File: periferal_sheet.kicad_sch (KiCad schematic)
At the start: 0 parts

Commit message: Troquei o micro para STM32H523, adicionei o cristal HSE, circuito da fonte de 5V e 3v3, CAN, SD
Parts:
- added J3: Conn_02x02_Counter_Clockwise, symbol Connector_Generic:Conn_02x02_Counter_Clockwise
- added JP2: SolderJumper_2_Open, Jumper:SolderJumper-2_P1.3mm_Open_RoundedPad1.0x1.5mm, symbol Jumper:SolderJumper_2_Open
- added R24: 10K, Resistor_SMD:R_1206_3216Metric, symbol Device:R
- added R25: 120, Resistor_SMD:R_1206_3216Metric, symbol Device:R
- added U12: SN65HVD230, Package_SO:SOIC-8_3.9x4.9mm_P1.27mm, symbol Interface_CAN_LIN:SN65HVD230
- added U13: ~, Baja_Librarys:SD-CARD-GENERIC, symbol Baja_Librarys:SD-CARD-GENERIC
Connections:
- new net: R24.1, U12.8 (Rs)
- new net: JP2.2 (B), R25.2
- new net +12V: J3.1 (Pin_1)
- new net +3V3: U12.3 (VCC)
- new net 3V3: U13.4 (VCC)
- new net CAN +: J3.3 (Pin_3), R25.1, U12.7 (CANH)
- new net CAN -: J3.4 (Pin_4), JP2.1 (A), U12.6 (CANL)
- new net CRX: U12.4 (R)
- new net CS_SD: U13.2 (DAT3/CS)
- new net CTX: U12.1 (D)
- new net GND: J3.2 (Pin_2), R24.2, U12.2 (GND), U13.6 (GND)
- new net GNDD: U13.10 (SH_1), U13.11 (SH_2), U13.12 (SH_3), U13.13 (SH_4)
- new net MISO: U13.7 (DAT0/MISO)
- new net MOSI: U13.3 (CMD/MOSI)
- new net SCK: U13.5 (CLK)
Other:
- note added: "Conector Molex"
- note added: "Conector SD-Card"
- note added: "Nota: Par diferencial do CAN"
- note added: "Transceiver CAN"

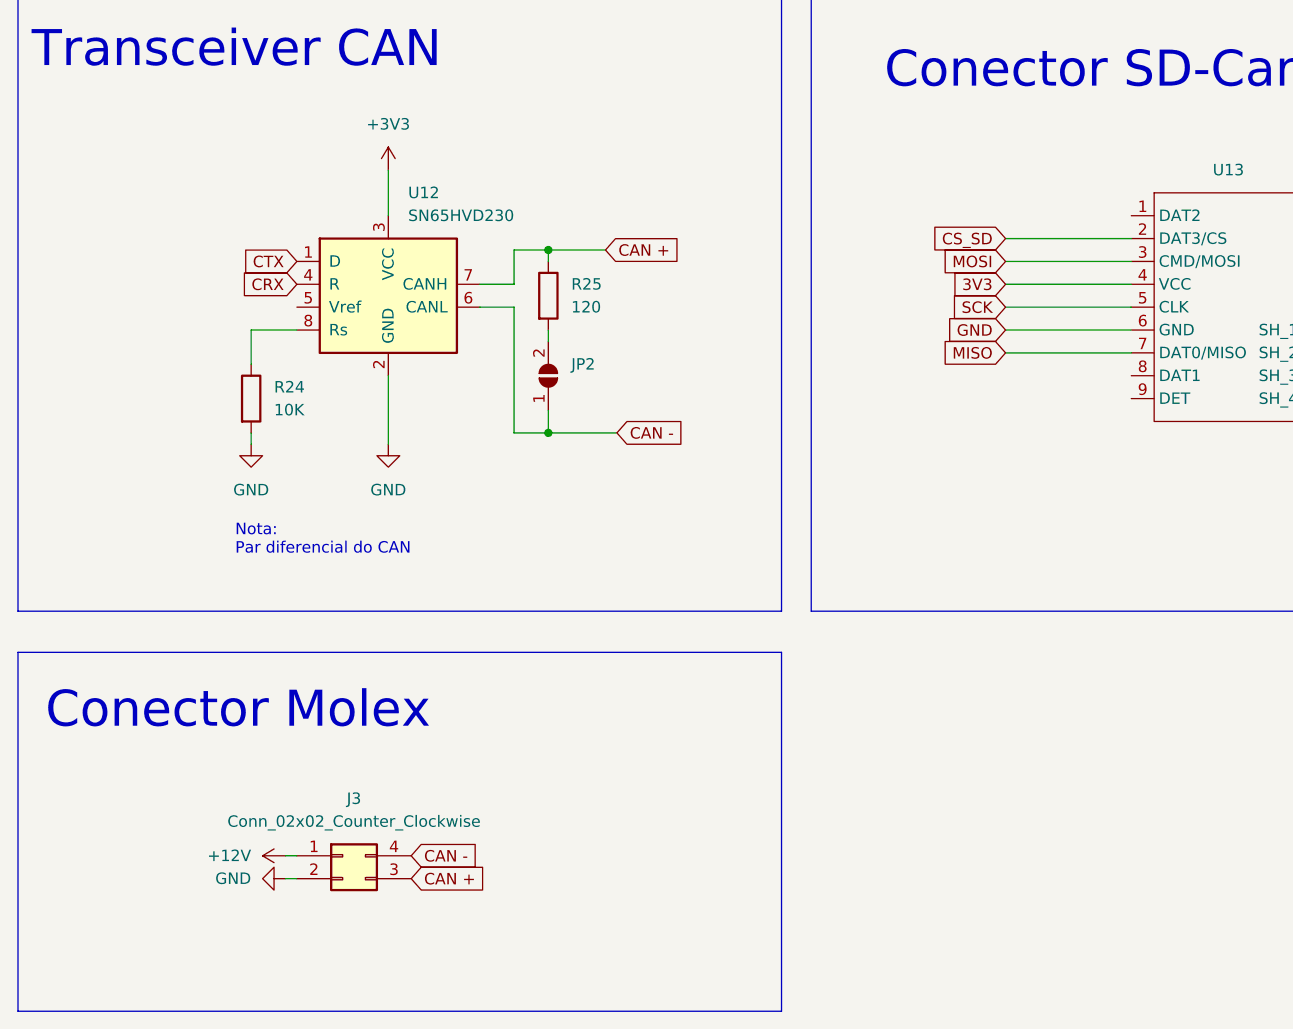
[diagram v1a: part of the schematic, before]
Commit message: Alterei o nome para o par diferencial do CAN, adicionei capacitores de desacoplamento para todas as alimentacoes
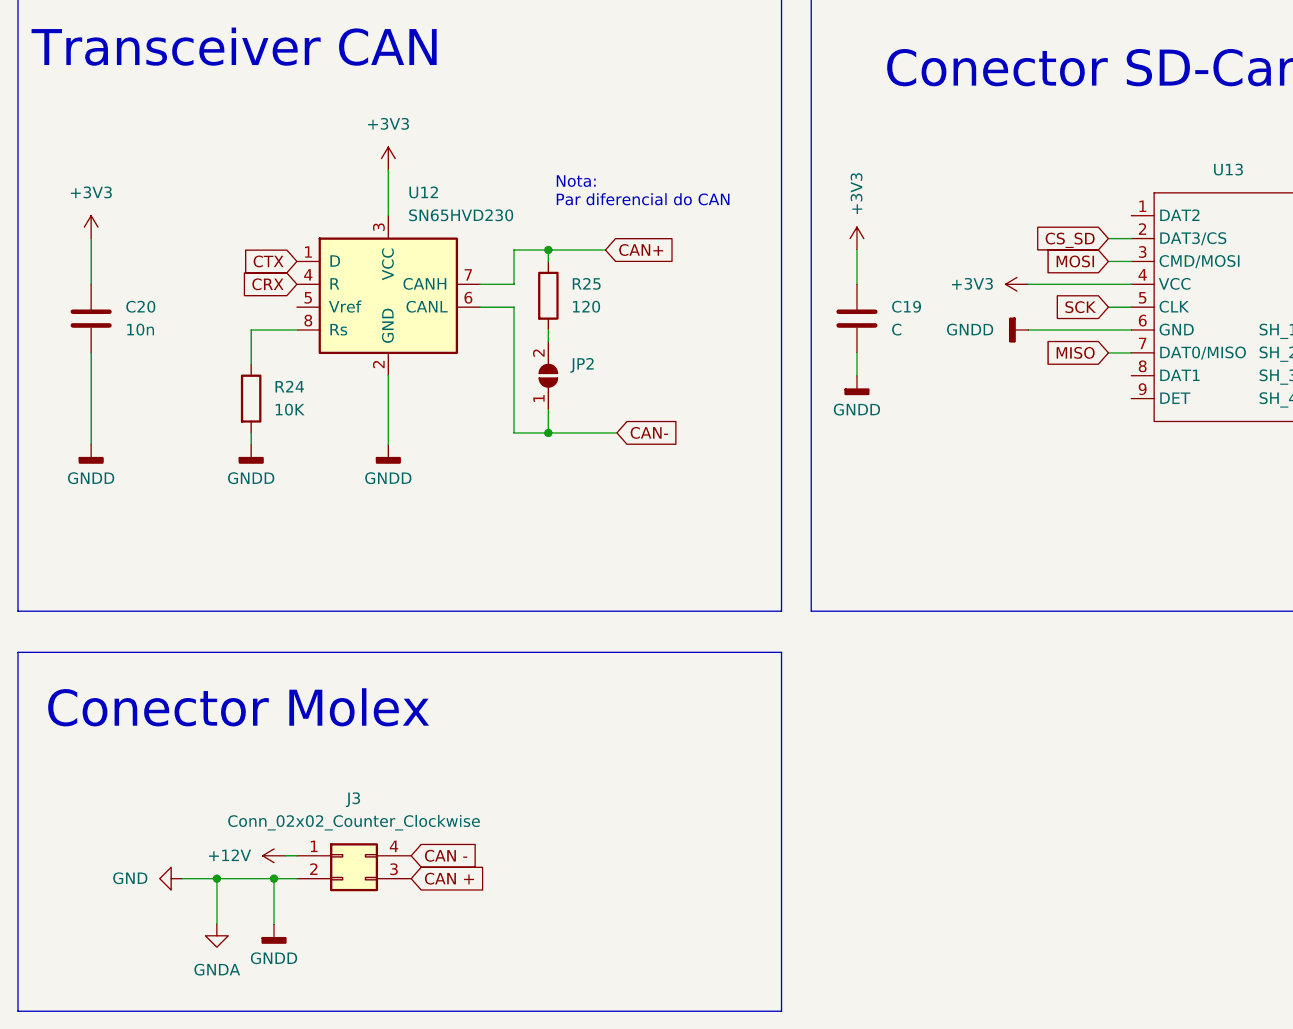
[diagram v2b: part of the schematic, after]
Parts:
- added C19: C, symbol Device:C
- added C20: 10n, symbol Device:C
- U13: footprint Baja_Librarys:SD-CARD-GENERIC -> BajaKICAD:SD-CARD-GENERIC
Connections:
- net 3V3 is gone; now on net +3V3: U13.4 (VCC)
- net GNDD is gone; now on net GND: U13.10 (SH_1), U13.11 (SH_2), U13.12 (SH_3), U13.13 (SH_4)
- net +3V3: now also C19.1, C20.1
- net CAN +: no longer R25.1, U12.7 (CANH)
- net CAN -: no longer JP2.1 (A), U12.6 (CANL)
- net GND: now also C19.2, C20.2
- new net CAN+: R25.1, U12.7 (CANH)
- new net CAN-: JP2.1 (A), U12.6 (CANL)

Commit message: Removi as entradas analógicas, projeto delas estava errado
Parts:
- removed J3: Conn_02x02_Counter_Clockwise, symbol Connector_Generic:Conn_02x02_Counter_Clockwise
- removed R25: 120, Resistor_SMD:R_1206_3216Metric, symbol Device:R
- added J3: Conn_02x02_Top_Bottom, Baja_Library:MX150L_4P, symbol Connector_Generic:Conn_02x02_Top_Bottom
- added R18: 120, Capacitor_SMD:C_0603_1608Metric_Pad1.08x0.95mm_HandSolder, symbol Device:R
- added R20: 10k, Resistor_SMD:R_1206_3216Metric_Pad1.30x1.75mm_HandSolder, symbol Device:R
- C19: renamed from C20; value 10n -> 1n; footprint (none) -> Capacitor_SMD:C_0603_1608Metric_Pad1.08x0.95mm_HandSolder
- C20: renamed from C19; value C -> 1n; footprint (none) -> Capacitor_SMD:C_0603_1608Metric_Pad1.08x0.95mm_HandSolder
- R19: renamed from R24; value 10K -> 10k; footprint Resistor_SMD:R_1206_3216Metric -> Resistor_SMD:R_1206_3216Metric_Pad1.30x1.75mm_HandSolder
- U13: footprint BajaKICAD:SD-CARD-GENERIC -> Baja_Library:SD-CARD-GENERIC
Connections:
- net +12V: now also J3.1 (Pin_1)
- net +3V3: now also R20.2
- net CAN+: now also J3.4 (Pin_4), R18.1
- net CAN-: now also J3.3 (Pin_3)
- net GND: now also J3.2 (Pin_2); no longer C19.2, C20.2, R19.2, U12.2 (GND), U13.10 (SH_1), U13.11 (SH_2), U13.12 (SH_3), U13.13 (SH_4), U13.6 (GND)
- net SD_ON: now reaches U13.9 (DET)
- net SD_ON: now also R20.1
- net at JP2.2 (B): now also R18.2
- new net GNDD: C19.2, C20.2, R19.2, U12.2 (GND), U13.10 (SH_1), U13.11 (SH_2), U13.12 (SH_3), U13.13 (SH_4), U13.6 (GND)
- no-connect marks 0 -> 2
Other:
- note added: "Nota: Permite diferentes tamanhos de resistor"
- note removed: "Nota: Par diferencial do CAN"
- moved on the sheet: JP2

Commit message: Alterei para ter 3 portas analogicas, adaptei o circuito do RPM para ter um jumper que permite usar como entrada digital
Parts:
- removed J3: Conn_02x02_Top_Bottom, Baja_Library:MX150L_4P, symbol Connector_Generic:Conn_02x02_Top_Bottom
- removed JP2: SolderJumper_2_Open, Jumper:SolderJumper-2_P1.3mm_Open_RoundedPad1.0x1.5mm, symbol Jumper:SolderJumper_2_Open
- removed R18: 120, Capacitor_SMD:C_0603_1608Metric_Pad1.08x0.95mm_HandSolder, symbol Device:R
- added C22, C24, C25: 22u, Capacitor_THT:CP_Radial_D6.3mm_P2.50mm, symbol Device:C
- added C23: 100n, Capacitor_SMD:C_0603_1608Metric_Pad1.08x0.95mm_HandSolder, symbol Device:C
- added D5: LED, Baja_Library:LED_1210_HandSoldering, symbol Device:LED
- added J2: Conn_02x06_Top_Bottom, Baja_Library:MX120G, symbol Connector_Generic:Conn_02x06_Top_Bottom
- added R15: 1k, Resistor_SMD:R_1206_3216Metric_Pad1.30x1.75mm_HandSolder, symbol Device:R
- added R16: 120, Capacitor_SMD:C_0603_1608Metric_Pad1.08x0.95mm_HandSolder, symbol Device:R
- added U10: AMS1117-3.3, Package_TO_SOT_SMD:SOT-223-3_TabPin2, symbol Regulator_Linear:AMS1117-3.3
- added U9: AMS1117-5.0, Package_TO_SOT_SMD:SOT-223-3_TabPin2, symbol Regulator_Linear:AMS1117-5.0
- renumbered C19 to C26, C20 to C27, R19 to R17, R20 to R18, U12 to U11, U13 to U12
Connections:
- net +12V: now also C22.1, J2.1 (Pin_1), U9.3 (VI)
- net +3V3: now also C25.1, R15.1, U10.2 (VO)
- net CAN+: now also J2.7 (Pin_7), R16.1
- net CAN-: now also J2.8 (Pin_8), R16.2
- net GND: now also C26.2, R17.2, U11.2 (GND), U12.10 (SH_1), U12.11 (SH_2), U12.12 (SH_3), U12.13 (SH_4), C22.2, C23.2, C24.2, C25.2, D5.1 (K), J2.2 (Pin_2), U10.1 (GND), U9.1 (GND)
- net GNDD: no longer C26.2, R17.2, U11.2 (GND), U12.10 (SH_1), U12.11 (SH_2), U12.12 (SH_3), U12.13 (SH_4)
- new net: D5.2 (A), R15.2
- new net +5V: C23.1, C24.1, U10.3 (VI), U9.2 (VO)
- new net CHASSI: J2.12 (Pin_12)
- new net MTMT: J2.6 (Pin_6)
- new net NTC_P1: J2.3 (Pin_3)
- new net NTC_P2: J2.4 (Pin_4)
- new net NTC_P3: J2.5 (Pin_5)
- new net OPTO_IN_0: J2.11 (Pin_11)
- new net OPTO_IN_1: J2.10 (Pin_10)
- new net OPTO_IN_2: J2.9 (Pin_9)
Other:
- note added: "Fonte 3V3 (LDO)"
- note added: "Fonte 5V (LDO)"
- note added: "LED da fonte"
- note added: "Nota: Capacitor "bulky" de desacoplamento é da entrada, o da saída já tem na fonte de 3v3"
- note added: "Nota: Capacitor 22uF recomendado pelo datasheet"
- note added: "Nota: Compatível com LDL1117 da ST"
- moved on the sheet: C26, C27, R17, R18, U11, U12

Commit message: Diminui o tamanho da placa
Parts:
- removed C27: 1n, Capacitor_SMD:C_0603_1608Metric_Pad1.08x0.95mm_HandSolder, symbol Device:C
- removed R18: 10k, Resistor_SMD:R_1206_3216Metric_Pad1.30x1.75mm_HandSolder, symbol Device:R
- removed U12: ~, Baja_Library:SD-CARD-GENERIC, symbol Baja_Librarys:SD-CARD-GENERIC
- added C20: 1n, Capacitor_SMD:C_0805_2012Metric_Pad1.18x1.45mm_HandSolder, symbol Device:C
- added R16: 10K, Resistor_SMD:R_1206_3216Metric_Pad1.30x1.75mm_HandSolder, symbol Device:R
- added U8: ~, Baja_Library:SD-CARD-GENERIC, symbol Baja_Librarys:SD-CARD-GENERIC
- R15: renamed from R16; footprint Capacitor_SMD:C_0603_1608Metric_Pad1.08x0.95mm_HandSolder -> Resistor_SMD:R_0603_1608Metric_Pad0.98x0.95mm_HandSolder
- renumbered C22 to C16, C23 to C17, C24 to C18, C25 to C19, C26 to C21, D5 to D7, R15 to R14, U9 to U6, U10 to U7, U11 to U9
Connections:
- net +3V3: now also C20.1, R16.2, U8.4 (VCC)
- net GND: now also C20.2, U8.10 (SH_1), U8.11 (SH_2), U8.12 (SH_3), U8.13 (SH_4), U8.6 (GND)
- net MISO: now also U8.7 (DAT0/MISO)
- net MOSI: now also U8.3 (CMD/MOSI)
- net SCK: now also U8.5 (CLK)
- net CHASSI renamed MT+
- net MTMT renamed MT-
- new net SD_CS: U8.2 (DAT3/CS)
- new net SD_DET: R16.1, U8.9 (DET)
- no-connect marks 2 -> 0
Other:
- note added: "Chassi"
- note added: "MataMotor"
- note removed: "Conector SD-Card"

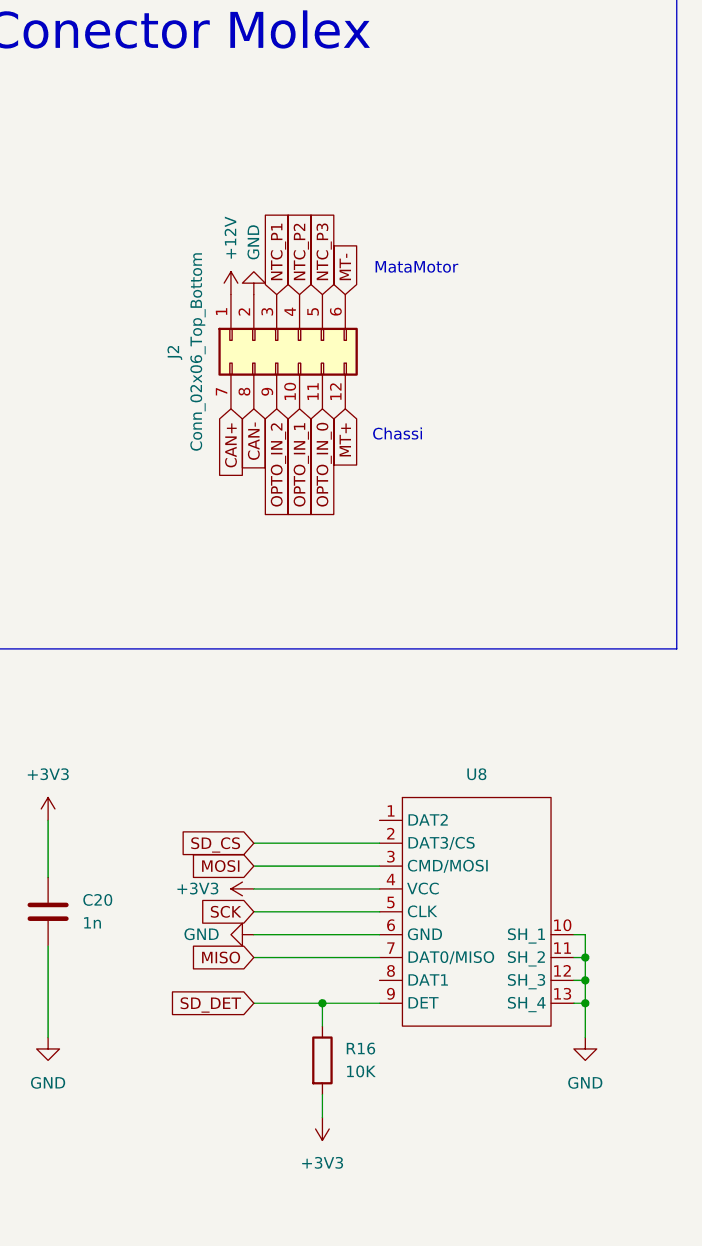
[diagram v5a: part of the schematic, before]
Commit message: Troquei o conector para o conector DEUTSCH
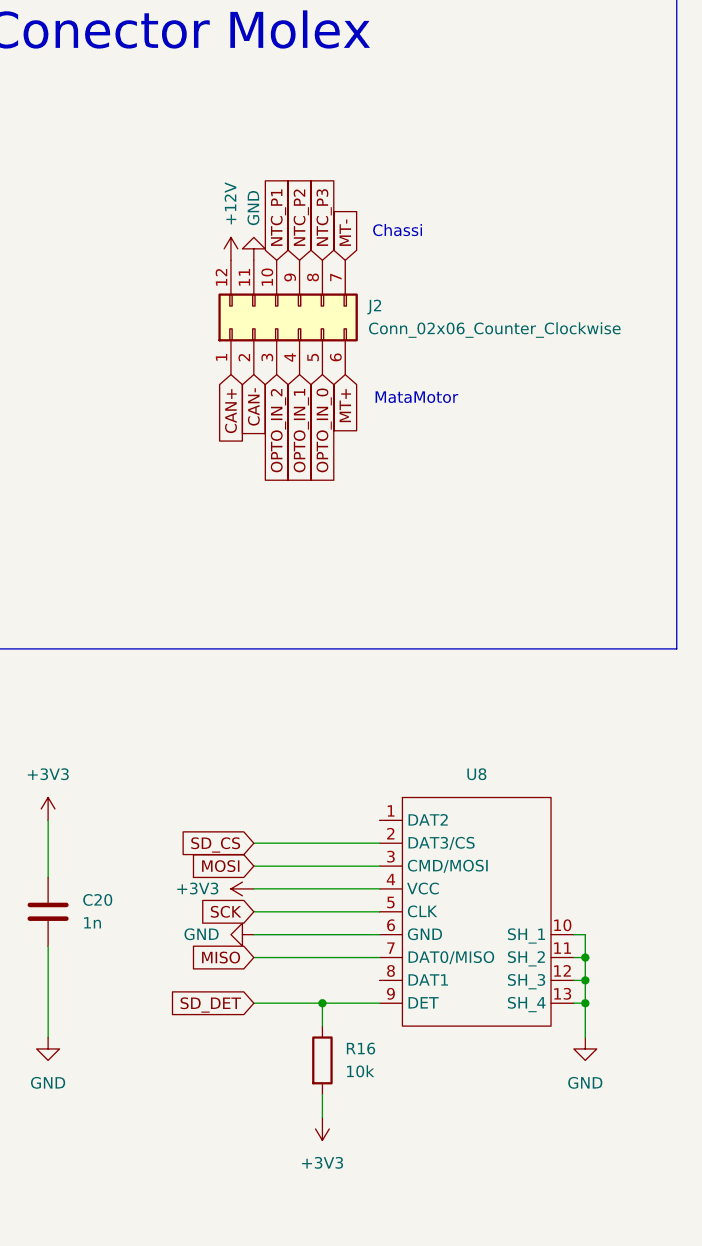
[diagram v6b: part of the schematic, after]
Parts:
- removed J2: Conn_02x06_Top_Bottom, Baja_Library:MX120G, symbol Connector_Generic:Conn_02x06_Top_Bottom
- added J2: Conn_02x06_Counter_Clockwise, Baja_Library:DTM1512PA, symbol Connector_Generic:Conn_02x06_Counter_Clockwise
- C20: footprint Capacitor_SMD:C_0805_2012Metric_Pad1.18x1.45mm_HandSolder -> Capacitor_SMD:C_0603_1608Metric_Pad1.08x0.95mm_HandSolder
- R16: value 10K -> 10k
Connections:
- net +12V: now also J2.12 (Pin_12)
- net CAN+: now also J2.1 (Pin_1)
- net CAN-: now also J2.2 (Pin_2)
- net GND: now also J2.11 (Pin_11)
- net MT+: now also J2.6 (Pin_6)
- net MT-: now also J2.7 (Pin_7)
- net NTC_P1: now also J2.10 (Pin_10)
- net NTC_P2: now also J2.9 (Pin_9)
- net NTC_P3: now also J2.8 (Pin_8)
- net OPTO_IN_0: now also J2.5 (Pin_5)
- net OPTO_IN_1: now also J2.4 (Pin_4)
- net OPTO_IN_2: now also J2.3 (Pin_3)
